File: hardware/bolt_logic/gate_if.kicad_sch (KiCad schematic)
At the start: 36 parts, among them CN2 SSW-120-01-T-D-LL, U4 74HCT573, U5 74HC21, U6 CD74HCT30

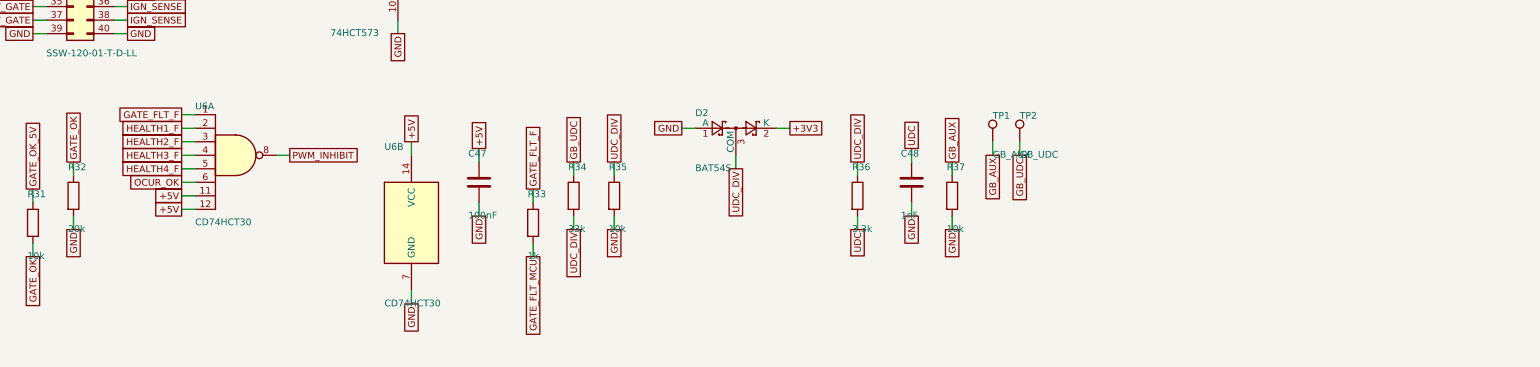
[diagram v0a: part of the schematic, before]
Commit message: Use JLCPCB-stocked parts: BTS6143D, 74HCT10, TCA0372 (schematic)
Owner-approved part changes so JLCPCB can assemble the board:
- Q1/Q2 BTS443P -> BTS6143D: same PG-TO252-5-11 pinout and IN-to-GND input, so the
  symbol, footprint and Q3/Q4 drive are unchanged (BOM only).
- U6 CD74HCT30 -> 74HCT10: PWM_INHIBIT = NAND(GATE_OK_5V, GATE_FLT_F, OCUR_OK), the
  same logic since U5 already ANDs HEALTH1-4.
- U13 L272D -> onsemi TCA0372DW (SOIC-16W), new custom symbol; exciter values unchanged.
- BOM: 3.3 nF C0G -> Murata GRM2165C1H332JA01D (previous choice out of stock);
  74HCT4052 -> TI CD74HCT4052M96 C469908 (confirmed listing); BTS133TC kept (owner).

The routed board and regenerated fab files follow once the routing run completes;
until then fab/ on this branch reflects the previous schematic.

Co-Authored-By: Claude Opus 5.5 <noreply@anthropic.com>
Claude-Session: https://claude.ai/code/session_01KW1M8KfVLc83FDDiK2YEWM
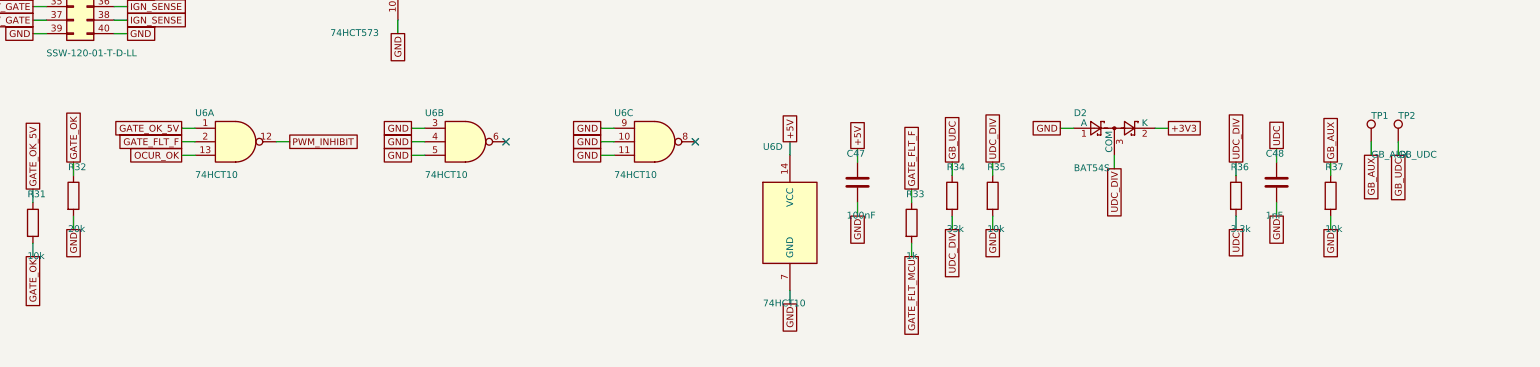
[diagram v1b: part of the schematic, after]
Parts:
- added unit 3 of U6
- added unit 4 of U6
- U6: value CD74HCT30 -> 74HCT10; symbol 74xx:74LS30 -> 74xx:74LS10
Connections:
- net +5V: now also U6.14 (VCC); no longer U6.11, U6.12, U6.14 (VCC)
- net GATE_FLT_F: now also U6.2; no longer U6.1
- net GATE_OK_5V: now also U6.1
- net GND: now also U6.3, U6.4, U6.5, U6.10, U6.11, U6.7 (GND), U6.9; no longer U6.7 (GND)
- net HEALTH1_F: no longer U6.2
- net HEALTH2_F: no longer U6.3
- net HEALTH3_F: no longer U6.4
- net HEALTH4_F: no longer U6.5
- net OCUR_OK: now also U6.13; no longer U6.6
- net PWM_INHIBIT: now also U6.12; no longer U6.8
- no-connect marks 5 -> 7
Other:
- moved on the sheet: C47, C48, D2, R33, R34, R35, R36, R37, TP1, TP2

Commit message: BOM: Littelfuse SMBJ26CA for TVS1, SN74ACT10 for U6 (stock)
JLCPCB is out of stock on the Bourns SMBJ26CA (C3719606) and the 74HCT10D (C547236).
- TVS1: Littelfuse SMBJ26CA C83332, same spec and SMB package.
- U6: TI SN74ACT10DR C2861739, same '10 pinout and SOIC-14; ACT has TTL-level inputs
  (VIH 2.0 V) like HCT, so the 3.3 V OCUR_OK line still reads high at 5 V.
No copper change: the routed board only gets U6's value updated; Gerber and drill
artwork is identical to the merged version apart from the generation dates. Schematic,
schematic PDF, fab BOM and docs regenerated.

Co-Authored-By: Claude Opus 5.5 <noreply@anthropic.com>
Claude-Session: https://claude.ai/code/session_01KW1M8KfVLc83FDDiK2YEWM
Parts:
- U6: value 74HCT10 -> SN74ACT10
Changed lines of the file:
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@@
         (font (size 1.27 1.27))
         (justify left)))
-    (property "Value" "74HCT10"
+    (property "Value" "SN74ACT10"
       (at 58.42 105.27 0)
       (effects
@@
         (font (size 1.27 1.27))
         (justify left)))
-    (property "Value" "74HCT10"
+    (property "Value" "SN74ACT10"
       (at 101.6 105.27 0)
       (effects
@@
         (font (size 1.27 1.27))
         (justify left)))
-    (property "Value" "74HCT10"
+    (property "Value" "SN74ACT10"
       (at 137.16 105.27 0)
       (effects
@@
         (font (size 1.27 1.27))
         (justify left)))
-    (property "Value" "74HCT10"
+    (property "Value" "SN74ACT10"
       (at 165.1 129.4 0)
       (effects
